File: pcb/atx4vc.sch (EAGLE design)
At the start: 76 parts, among them IC2 REG1117, IC3 STM32F042F4, IC4 MY_7905DT, J1 ATX24RH, SW1 324_SW, SW2 324_SW, SW3 324_SW, SW4 324_SW, SW5 324_SW, SW7 324_SW, U1 USBC_16P, U2 USBC_16P

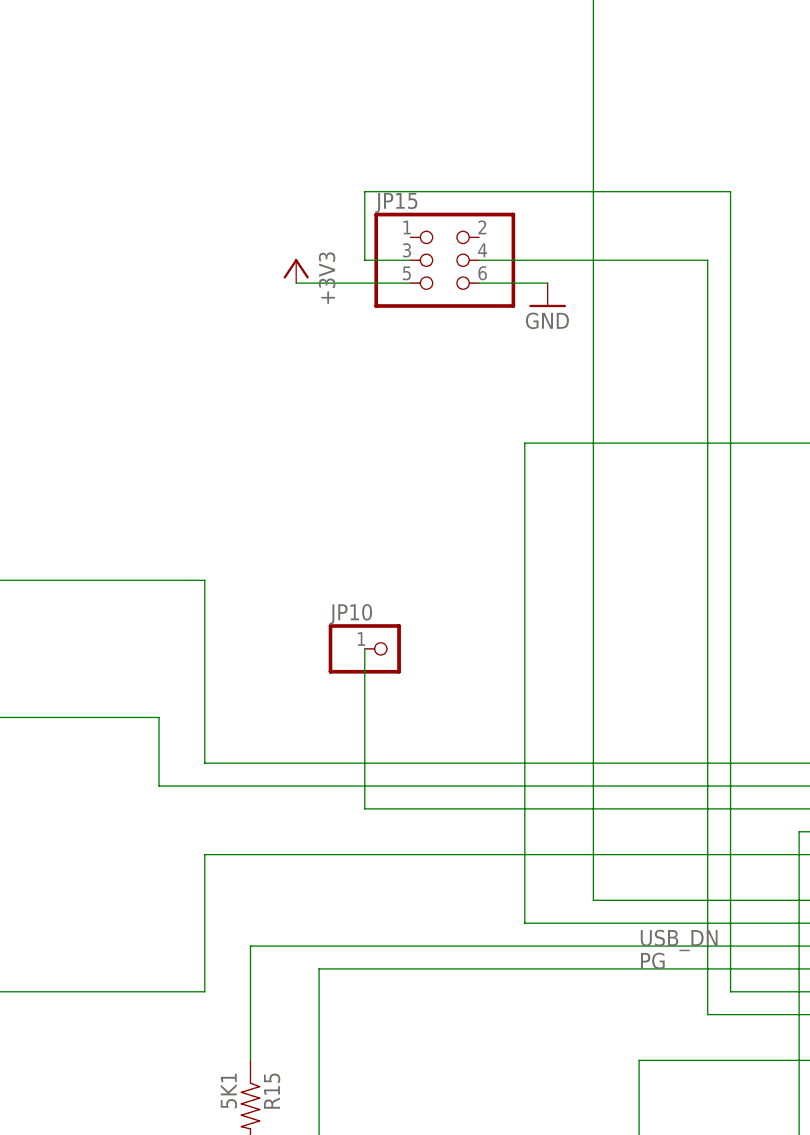
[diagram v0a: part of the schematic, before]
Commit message: adding power connector and fuse detect
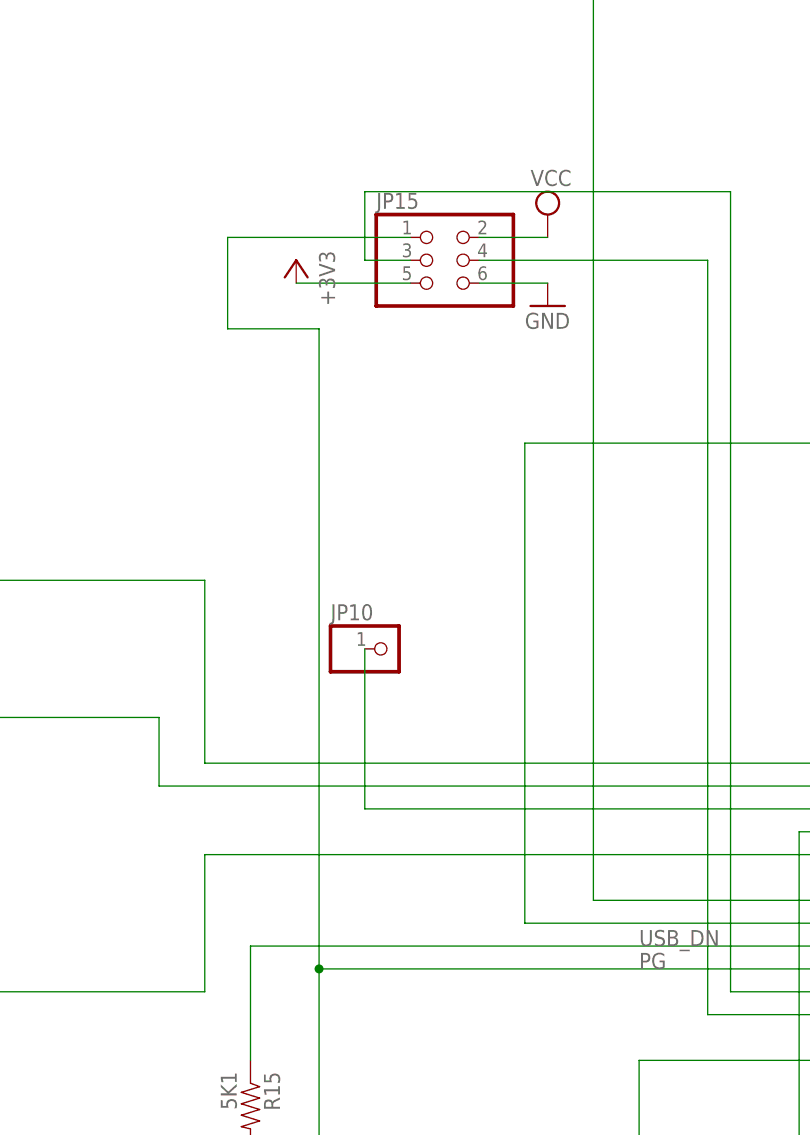
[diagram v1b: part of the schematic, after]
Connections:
- net PG: now also JP15.1
- net VCC: now also JP15.2
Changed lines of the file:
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@@
 <part name="GND41" library="backplane" deviceset="GND" device=""/>
 <part name="R22" library="atx_power_control" deviceset="RESISTOR" device="0805-RES" value="5K1"/>
+<part name="SUPPLY3" library="supply2" library_urn="urn:adsk.eagle:library:372" deviceset="VCC" device=""/>
 </parts>
 <sheets>
@@
 <attribute name="NAME" x="313.9186" y="77.47" size="1.778" layer="95" rot="R270"/>
 <attribute name="VALUE" x="309.118" y="77.47" size="1.778" layer="96" rot="R270"/>
+</instance>
+<instance part="SUPPLY3" gate="G$1" x="-50.8" y="101.6" smashed="yes">
+<attribute name="VALUE" x="-52.705" y="104.775" size="1.778" layer="96"/>
 </instance>
 </instances>
@@
 <wire x1="-86.36" y1="160.02" x2="-86.36" y2="154.94" width="0.1524" layer="91"/>
 </segment>
+<segment>
+<pinref part="JP15" gate="A" pin="2"/>
+<pinref part="SUPPLY3" gate="G$1" pin="VCC"/>
+<wire x1="-58.42" y1="99.06" x2="-50.8" y2="99.06" width="0.1524" layer="91"/>
+</segment>
 </net>
 <net name="N$2" class="0">
@@
 <wire x1="254" y1="-78.74" x2="-76.2" y2="-78.74" width="0.1524" layer="91"/>
 <wire x1="-76.2" y1="-78.74" x2="-76.2" y2="17.78" width="0.1524" layer="91"/>
-</segment>
-</net>
+<wire x1="-76.2" y1="17.78" x2="-76.2" y2="88.9" width="0.1524" layer="91"/>
+<wire x1="-76.2" y1="88.9" x2="-86.36" y2="88.9" width="0.1524" layer="91"/>
+<junction x="-76.2" y="17.78"/>
+<wire x1="-86.36" y1="88.9" x2="-86.36" y2="99.06" width="0.1524" layer="91"/>
+<pinref part="JP15" gate="A" pin="1"/>
+<wire x1="-86.36" y1="99.06" x2="-66.04" y2="99.06" width="0.1524" layer="91"/>
+</segment>
+</net>
